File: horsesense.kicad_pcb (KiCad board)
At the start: 4 copper layers, 30 x 60 mm, 67 parts, among them IC1 BGA824N6E6329XTSA1, J1 USB4105-GF-A-120, J2 S2B-PH-SM4-TB, J3 73412-0110, J4 Conn_01x04, SW1 EVQ-P7A01P, SW2 EVQ-P7A01P, U1 MAX86141ENP+T, U10 MAX-M8Q, U2 TXB0304RUTR, U3 BQ25601, U4 XC6210B332MR, U5 XC6210B182MR, U8 MX25L3233FM2I-08G, U9 ESP32-S3-WROOM-1-N16R8

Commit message: Update for JLC parts
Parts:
- removed C7: 22µ, Capacitor_SMD:C_0805_2012Metric
- C6: value 22µ -> 100n
- D1, D2, D3: value CT DBLP31.12-6C5D-56-J6U6-20-R18 -> JNJ-LTJG0106W15; footprint Local:CTDBLP31126C5D56J6U620R18 -> LED_SMD:LED_PLCC_2835
- J1: value USB4105-GF-A-120 -> 1054500101
- SW1, SW2: value EVQ-P7A01P -> EVQP7A01P
- moved C5 4.73 mm to (153.7, 113.0), turned to 180 degrees
- moved C6 1.19 mm to (153.7, 110.7)
- moved TP1 0.84 mm to (149.9, 115.5)
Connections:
- C6 pad 1: +3.3V -> +1.8V
- D1 pad 1: Net-(D1-K) -> +3.3V_LED
- D1 pad 2: +3.3V_LED -> Net-(D1-K)
- D2 pad 1: Net-(D2-K) -> +3.3V_LED
- D2 pad 2: +3.3V_LED -> Net-(D2-K)
- D3 pad 1: Net-(D3-K) -> +3.3V_LED
- D3 pad 2: +3.3V_LED -> Net-(D3-K)
- U1 pad A1: +3.3V -> +3.3V_LED
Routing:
- net +3.3V_LED: track 6.05 -> 16.0 mm, vias 4 -> 5
- net +3.3V: track 50.5 -> 43.7 mm, vias 13 -> 12
- net +1.8V: track 14.4 -> 18.8 mm
- net MAX_MOSI_1_8: track 13.3 -> 9.52 mm
- net Net-(D2-K): track 16.7 -> 19.7 mm, vias 1 -> 3
- net Net-(U1-PD1_IN): track 18.1 -> 16.4 mm
- net Net-(D1-K): track 4.79 -> 6.02 mm
- net GND: track 63.1 -> 63.8 mm, vias 42 -> 41
- net Net-(D3-K): track 29.7 -> 29.0 mm, vias 3 -> 1

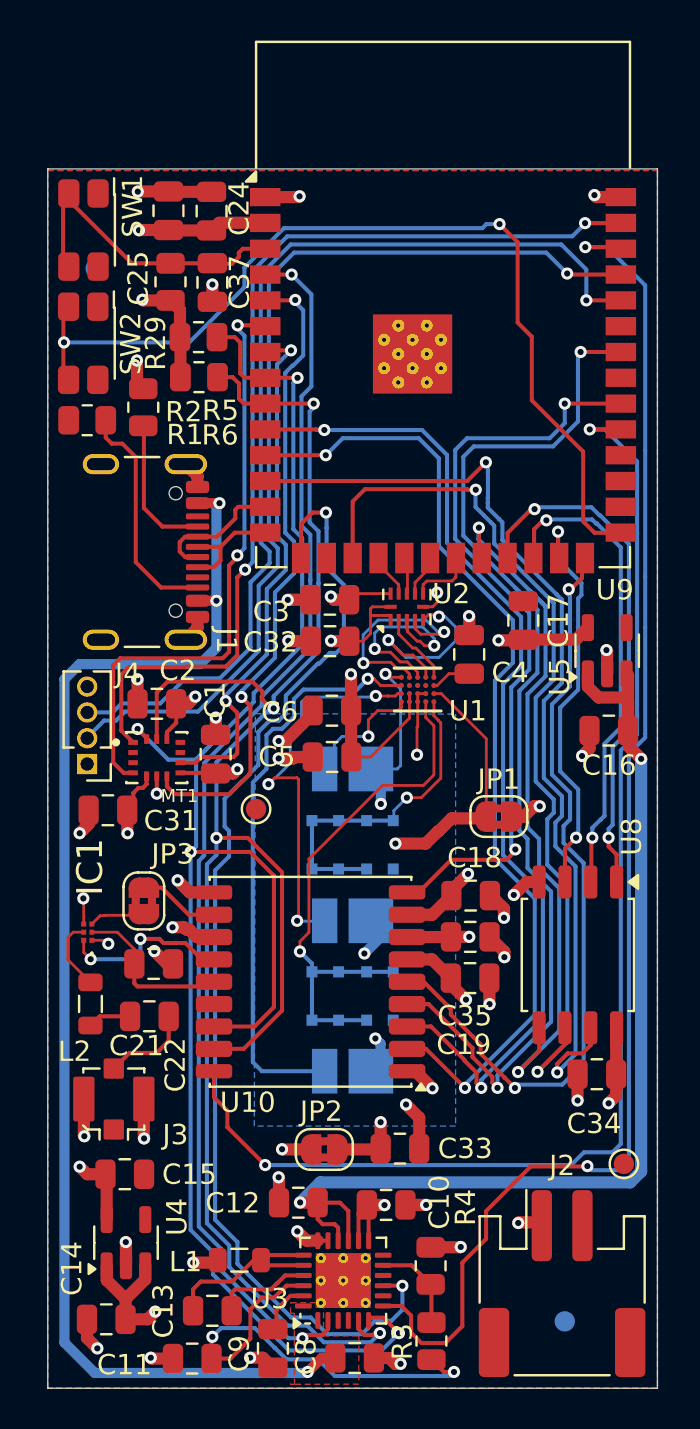
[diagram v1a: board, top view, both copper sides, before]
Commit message: Add red and IR LED for capter
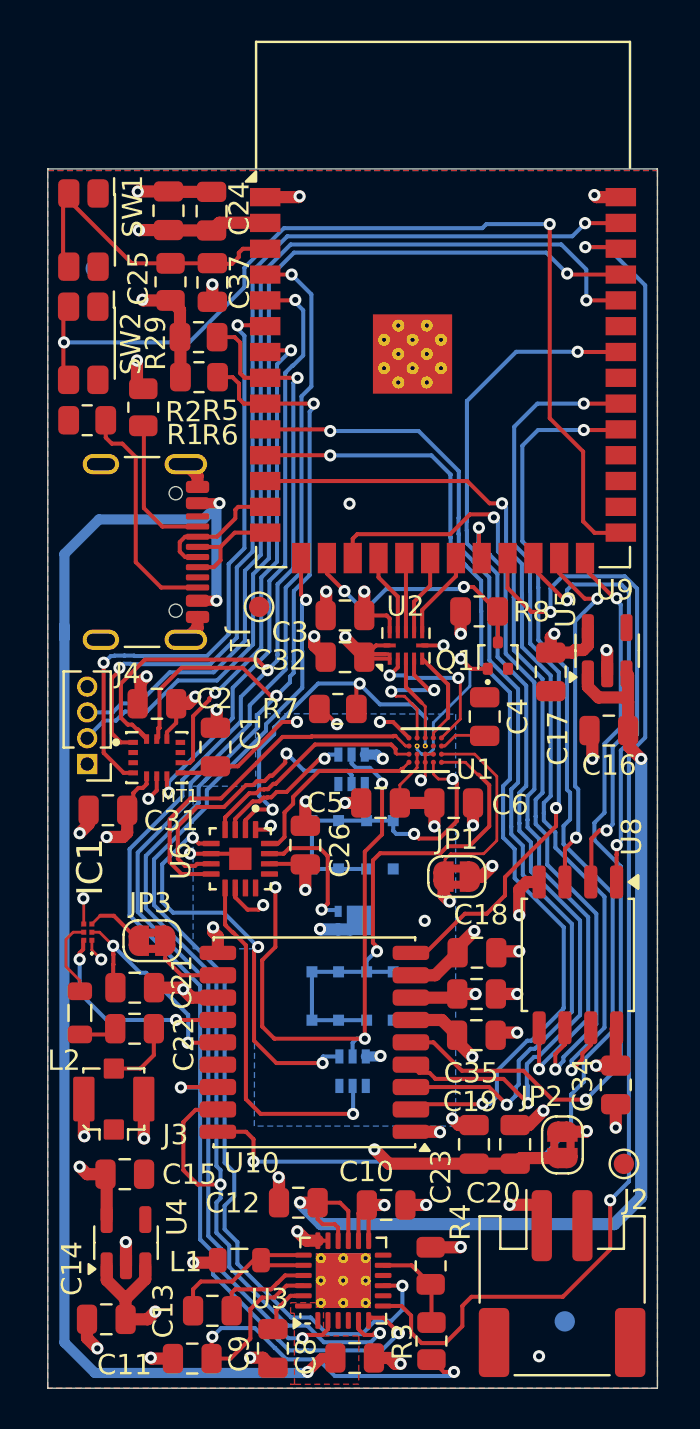
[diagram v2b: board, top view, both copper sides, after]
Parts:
- removed C33: 10µ, Capacitor_SMD:C_0805_2012Metric
- added C20: 22µ, Capacitor_SMD:C_0805_2012Metric, F.Cu at (162.7, 132.0)
- added C23: 22µ, Capacitor_SMD:C_0805_2012Metric, F.Cu at (160.7, 132.0)
- added C26: 22µ, Capacitor_SMD:C_0805_2012Metric, F.Cu at (152.4, 117.3)
- added Q1: RE1C002UNTCL, Package_TO_SOT_SMD:SOT-416, F.Cu at (161.8, 108.0)
- added R7: 100k, Resistor_SMD:R_0805_2012Metric, F.Cu at (154.0, 110.6)
- added R8: 100k, Resistor_SMD:R_0805_2012Metric, F.Cu at (160.9, 105.8)
- added U6: MAX4740ETE_, Local:QFN50P300X300X80-17N, F.Cu at (149.2, 118.0)
- D1: value JNJ-LTJG0106W15 -> CT DBLP31.12-6C5D-56-J6U6-20-R18; footprint LED_SMD:LED_PLCC_2835 -> Local:CTDBLP31126C5D56J6U620R18
- D2, D3: value JNJ-LTJG0106W15 -> SFH 7016; footprint LED_SMD:LED_PLCC_2835 -> Local:SFH7016
- moved JP2 11.7 mm to (165.0, 132.0), turned to 90 degrees
- moved TP1 9.95 mm to (150.1, 105.6)
- moved C6 7.52 mm to (159.7, 115.2), turned to 0 degrees
- moved D2 7.46 mm to (154.6, 113.6)
- moved D1 7.45 mm to (154.7, 121.0), turned to 0 degrees
- moved JP1 3.61 mm to (159.8, 118.8)
- moved C5 3.29 mm to (156.1, 115.2)
- moved C4 3.15 mm to (161.2, 111.0)
- moved U1 3.00 mm to (158.3, 112.6)
- moved U10 2.99 mm to (152.8, 127.0)
- moved C17 2.87 mm to (164.4, 108.8), turned to -90 degrees
- moved C18 2.83 mm to (160.8, 122.6)
- moved C19 2.83 mm to (160.8, 126.7)
- moved C35 2.83 mm to (160.8, 124.6)
- moved JP3 2.00 mm to (144.8, 122.0), turned to 180 degrees
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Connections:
- D2 pad 1: +3.3V_LED -> Net-(D2-RK)
- D2 pad 2: Net-(D2-K) -> +3.3V_LED
- D3 pad 1: +3.3V_LED -> Net-(D3-RK)
- D3 pad 2: Net-(D3-K) -> +3.3V_LED
- D4 pad 1: Net-(U1-PD2_IN) -> Net-(U1-PD1_IN)
- D4 pad 2: Net-(U1-PD2_IN) -> Net-(U1-PD1_IN)
- D4 pad 3: Net-(U1-PD2_IN) -> Net-(U1-PD1_IN)
- D4 pad 4: Net-(U1-PD2_IN) -> Net-(U1-PD1_IN)
- D4 pad 6: Net-(U1-PD2_IN) -> Net-(U1-PD1_IN)
- D4 pad 7: Net-(U1-PD2_IN) -> Net-(U1-PD1_IN)
- D4 pad 8: Net-(U1-PD2_IN) -> Net-(U1-PD1_IN)
- D6 pad 1: Net-(U1-PD1_IN) -> Net-(U1-PD2_IN)
- D6 pad 2: Net-(U1-PD1_IN) -> Net-(U1-PD2_IN)
- D6 pad 3: Net-(U1-PD1_IN) -> Net-(U1-PD2_IN)
- D6 pad 4: Net-(U1-PD1_IN) -> Net-(U1-PD2_IN)
- D6 pad 6: Net-(U1-PD1_IN) -> Net-(U1-PD2_IN)
- D6 pad 7: Net-(U1-PD1_IN) -> Net-(U1-PD2_IN)
- D6 pad 8: Net-(U1-PD1_IN) -> Net-(U1-PD2_IN)
- U1 pad B1: Net-(D3-K) -> Net-(U1-LED3_DRV)
- U1 pad B2: unconnected-(U1-*INT-PadB2) -> MAX_INT_1_8
- U1 pad B3: unconnected-(U1-GPIO1-PadB3) -> GPIO1
- U1 pad C1: Net-(D2-K) -> Net-(U1-LED2_DRV)
- U1 pad D1: Net-(D1-K) -> Net-(U1-LED1_DRV)
- U9 pad 16: unconnected-(U9-IO46-Pad16) -> MAX_INT
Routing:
- net Net-(D2-GK): track 0.00 -> 33.1 mm, vias 0 -> 4
- net Net-(D3-K): track 29.0 -> 0.00 mm, vias 1 -> 0
- net GPIO1: track 0.00 -> 26.6 mm, vias 0 -> 3
- net Net-(D3-RK): track 0.00 -> 20.2 mm, vias 0 -> 3
- net Net-(D2-K): track 19.7 -> 0.00 mm, vias 3 -> 0
- net Net-(U1-LED3_DRV): track 0.00 -> 18.1 mm
- net Net-(D3-BK): track 0.00 -> 17.8 mm, vias 0 -> 1
- net Net-(D2-BK): track 0.00 -> 14.7 mm, vias 0 -> 1
- net MAX_INT: track 0.00 -> 12.1 mm, vias 0 -> 2
- net Net-(U1-LED2_DRV): track 0.00 -> 11.4 mm
- net Net-(U1-PD1_IN): track 16.4 -> 26.1 mm
- net Net-(U1-PD2_IN): track 26.7 -> 17.0 mm, vias 1 -> 2
- net Net-(U1-LED1_DRV): track 0.00 -> 9.43 mm
- net MAX_INT_1_8: track 0.00 -> 8.12 mm, vias 0 -> 1
- net +3.3V: track 43.7 -> 50.7 mm, vias 12 -> 13
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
